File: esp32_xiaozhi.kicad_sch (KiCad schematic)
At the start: 0 parts

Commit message: Add components: TXS0108E, FT232 oscillators/power/USB, symbol library table
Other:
- added sheet TXS0108E (TXS0108E.kicad_sch)
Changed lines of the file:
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@@
+	)
+	(sheet
+		(at 80.01 40.64)
+		(size 48.26 38.1)
+		(exclude_from_sim no)
+		(in_bom yes)
+		(on_board yes)
+		(dnp no)
+		(fields_autoplaced yes)
+		(stroke
+			(width 0.1524)
+			(type solid)
+		)
+		(fill
+			(color 0 0 0 0)
+		)
+		(property "Sheetname" "TXS0108E"
+			(at 80.01 39.9284 0)
+			(show_name no)
+			(do_not_autoplace no)
+			(effects
+				(font
+					(size 1.27 1.27)
+				)
+				(justify left bottom)
+			)
+		)
+		(property "Sheetfile" "TXS0108E.kicad_sch"
+			(at 80.01 79.3246 0)
+			(show_name no)
+			(do_not_autoplace no)
+			(effects
+				(font
+					(size 1.27 1.27)
+				)
+				(justify left top)
+			)
+		)
+		(instances
+			(project "esp32_xiaozhi"
+				(path "/cae338e8-f342-43cb-b99a-a0486629133c"
+					(page "13")
+				)
+			)
+		)
 	)
 	(sheet

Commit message: ESP32S3 branch initial changes
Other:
- sheet esp32_c6 renamed esp32_C6
- added sheet Battery (Battery.kicad_sch)
- added sheet esp32_s3 (esp32_S3.kicad_sch)
- sheet TXS0108E ports: added A1, A2, A3, A4, A5, A6, A7, A8, B1, B2, B3, B4, B5, B6, B7, B8, OE; removed none
- sheet inmp441 ports: added EN, L/R, SCK, SD, WS; removed none

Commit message: ESP32S3 push before GPIO label changes
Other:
- removed sheet esp32_C6
- sheet Battery ports: added PCF85263_SCL, PCF85263_SDA; removed none
- sheet display ports: added BLK, CLK, DC, DI, RES, scl, sda; removed none
- sheet ft232 ports: added FT_CTS, FT_DTR, FT_RX, FT_TX, FT_VCC, mclr; removed none
- sheet led_sw_gpio ports: added led3, led4, led5, led6, sw1, sw2, sw3, sw4, sw5, sw6, sw7, sw8; removed none
- sheet max98357a ports: added BCLK, DIN, GAIN, LRC, PAD, SD; removed none

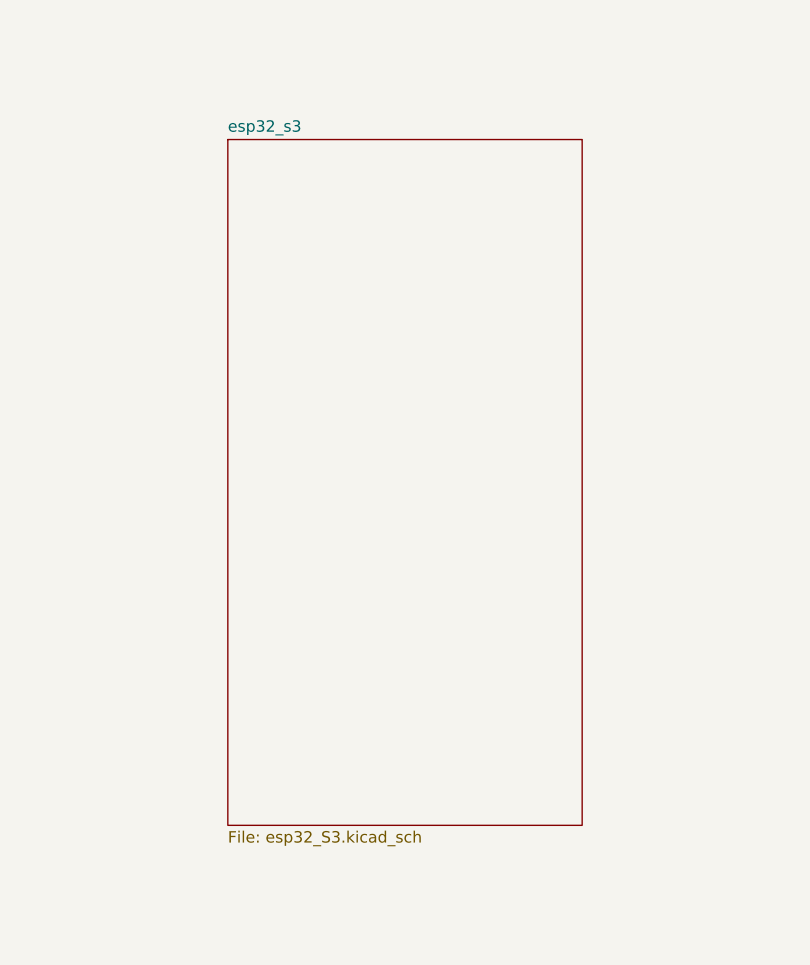
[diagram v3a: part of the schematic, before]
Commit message: ESP32S3: rename hierarchical GPIO labels and remove PCB tracks
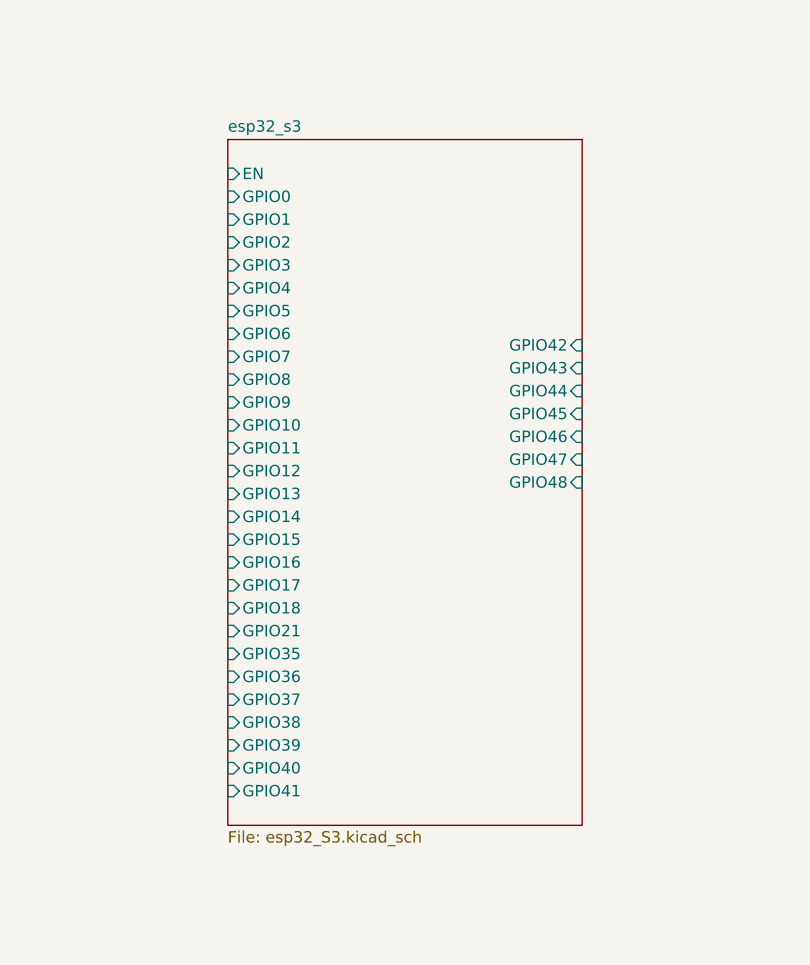
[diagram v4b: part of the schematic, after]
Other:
- sheet esp32_s3 ports: added EN, GPIO0, GPIO1, GPIO10, GPIO11, GPIO12, GPIO13, GPIO14, GPIO15, GPIO16, GPIO17, GPIO18, GPIO2, GPIO21, GPIO3, GPIO35, GPIO36, GPIO37, GPIO38, GPIO39, GPIO4, GPIO40, GPIO41, GPIO42, GPIO43, GPIO44, GPIO45, GPIO46, GPIO47, GPIO48, GPIO5, GPIO6, GPIO7, GPIO8, GPIO9; removed none

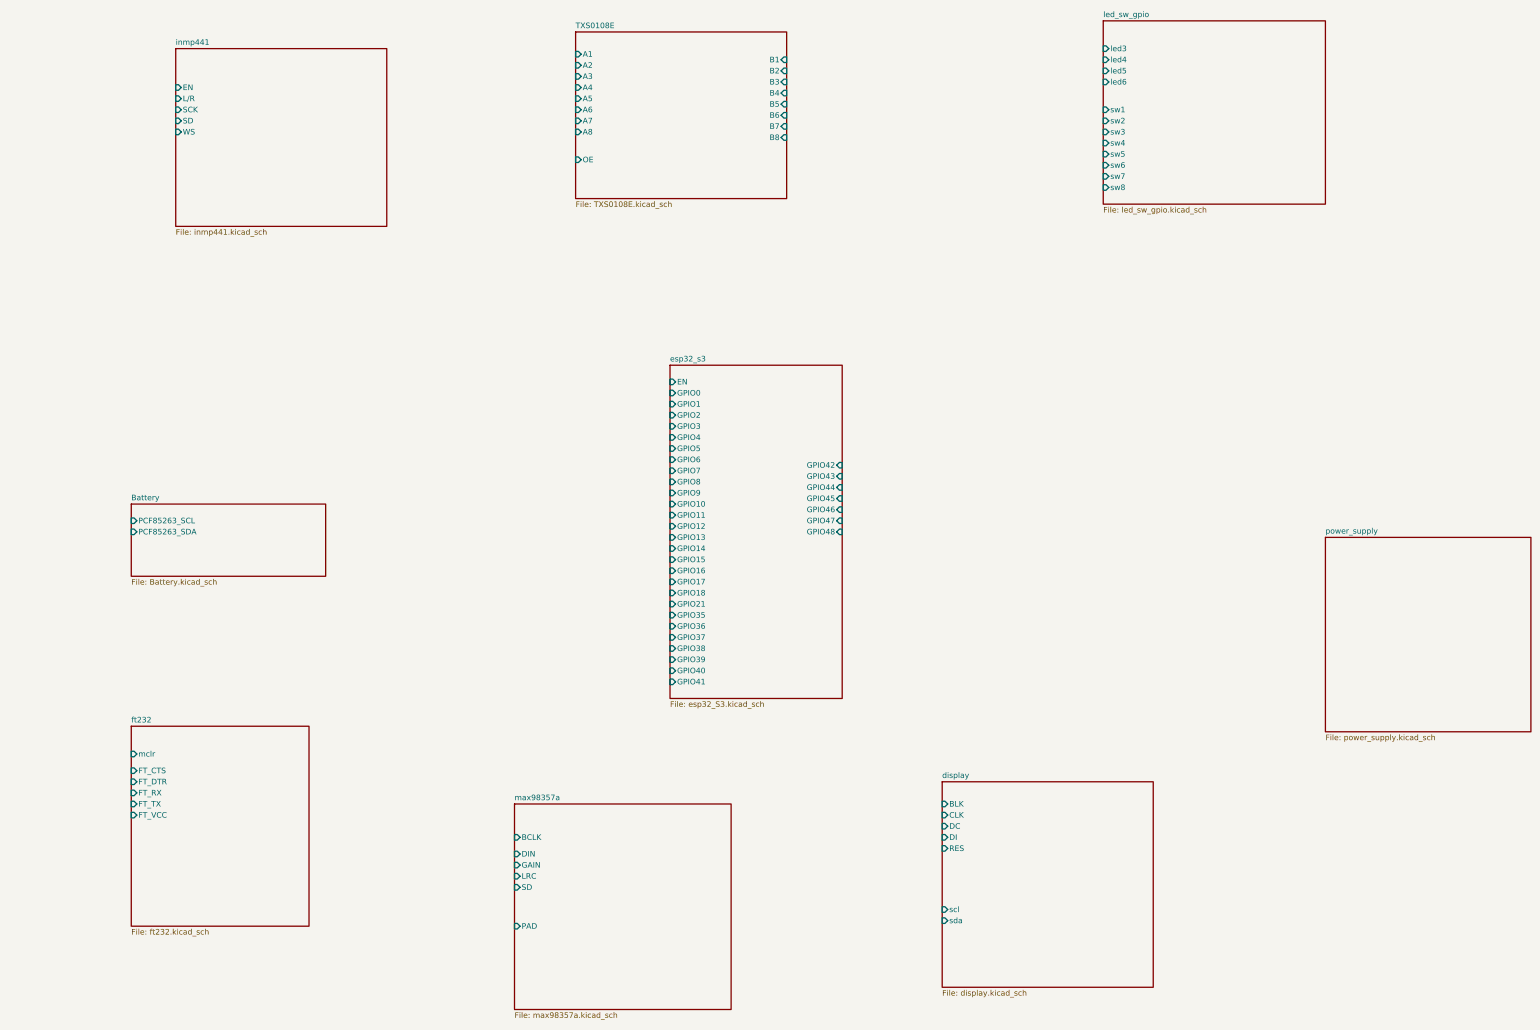
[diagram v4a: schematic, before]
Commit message: Actualización de esquemáticos y PCB
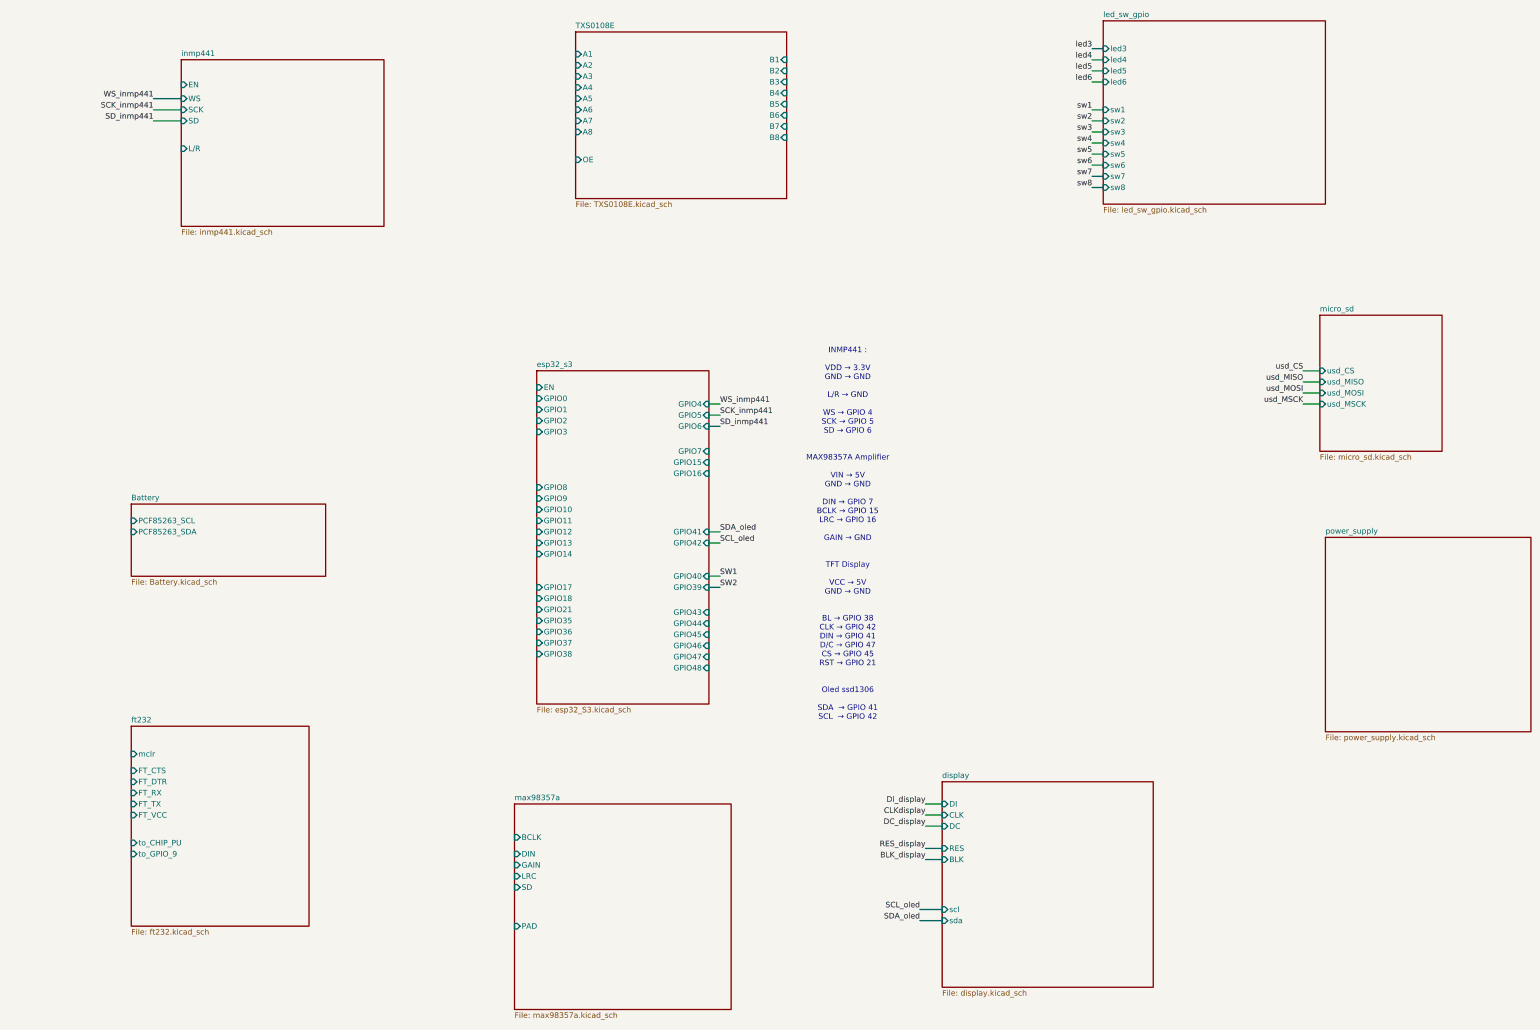
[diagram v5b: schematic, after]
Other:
- added sheet micro_sd (micro_sd.kicad_sch)
- sheet ft232 ports: added to_CHIP_PU, to_GPIO_9; removed none
- note added: "INMP441 : VDD → 3.3V GND → GND L/R → GND WS → GPIO 4 SCK → GPIO 5 SD → GPIO 6 MAX98357A Amplifier VIN → 5V GND → GND DIN → GPIO 7 BCLK → GPIO 15 LRC → GPIO 16 GAIN → GND TFT Display VCC → 5V GND → GND BL → GPIO 38 CLK → GPIO 42 DIN → GPIO 41 D/C → GPIO 47 CS → GPIO 45 RST → GPIO 21 Oled ssd1306 SDA → GPIO 41 SCL → GPIO 42"
